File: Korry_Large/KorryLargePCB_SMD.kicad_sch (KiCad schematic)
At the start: 9 parts, among them J1 BTN+LED, J2 BK_LED

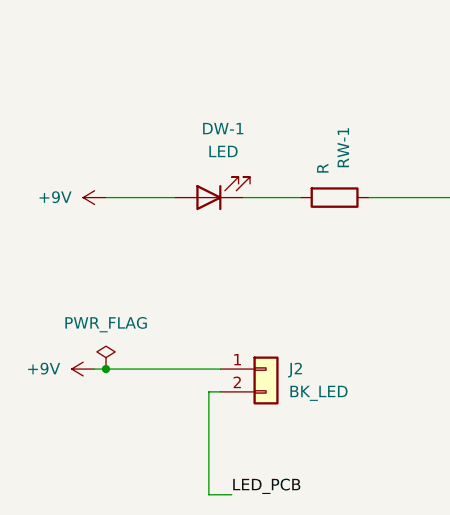
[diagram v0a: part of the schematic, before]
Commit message: Fix the swapped EFIS filenames and rename the backlight nets to +5V
Two naming defects, no electrical change on any board.

EFIS sheets
-----------
The root sheet pointed EFIS_LEFT at efis_right.kicad_sch and EFIS_RIGHT at
efis_left.kicad_sch. The schematic was correct, since the file behind the
LEFT sheet did hold the L_* signals, but the filenames said the opposite and
anyone reading the files from outside KiCad would have been misled.

The two files are swapped and every reference follows: the sheet properties
in the root schematic and the 49 sheetfile entries the footprints carry on
the board. Each file now matches the sheet that loads it.

  netlist   198 nets, 135 components, not one node moved
  ERC       0 violations
  DRC       6 violations, all cosmetic, 0 unconnected, 0 parity issues

Backlight nets
--------------
Every net in the backlighting chain was called +9V while carrying 5 V, on
all four boards. The white LEDs sit behind 91 Ω: at 5 V that is 21 mA, right
at the rating for a 1206 white LED, while 9 V would put them at 65 mA. The
name was a leftover from an earlier design and was the kind of label that
eventually makes someone connect the wrong supply.

Renamed across Korry_Large, Korry_Small, Backlighting_Dimmer and
Backlighting_LEDModule, in both the schematics and the boards: the power
symbol, its value, which is what actually names the net, and the net entries
on the copper. 88 occurrences. None of those boards had a +5V net already,
so nothing was merged.

Verified against the state committed a moment ago: ERC and DRC counts are
identical on all four boards, before and after, and no board gained or lost
a connection.

The Readme drops these two entries and gains the defects that surfaced while
checking: the Backlighting_Dimmer footprints carry their reference in the
value field instead of the schematic value, so a BOM read from that board is
wrong; its terminal block footprint no longer exists in the KiCad library;
four texts on the Korry_Large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
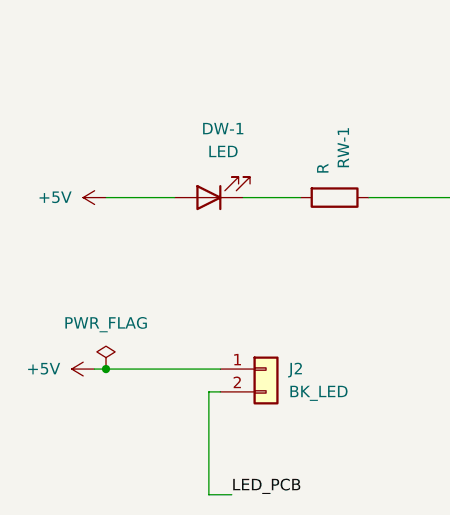
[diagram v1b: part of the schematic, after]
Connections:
- net +9V renamed +5V
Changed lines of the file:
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@@
 	)
 	(symbol
-		(lib_id "power:+9V")
+		(lib_id "power:+5V")
 		(at 72.39 99.06 90)
 		(unit 1)
@@
 			)
 		)
-		(property "Value" "+9V"
+		(property "Value" "+5V"
 			(at 68.58 99.06 90)
 			(effects
@@
 	)
 	(symbol
-		(lib_id "power:+9V")
+		(lib_id "power:+5V")
 		(at 71.12 118.11 90)
 		(unit 1)
@@
 			)
 		)
-		(property "Value" "+9V"
+		(property "Value" "+5V"
 			(at 67.31 118.11 90)
 			(effects

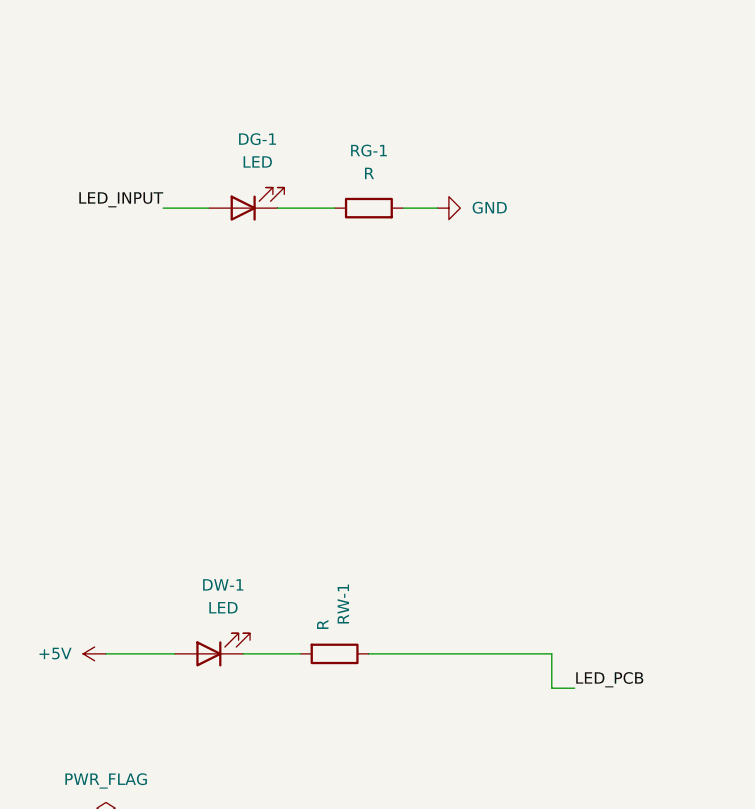
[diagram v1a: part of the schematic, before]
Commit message: Re-annotate the dimmer against its board, set the Korry resistor values
Tidying only. No board changed, no connection moved: all six projects still
report 0 unconnected items and 0 schematic parity issues.

Backlighting_Dimmer was worse than the value mismatch the Readme recorded.
Its schematic and its board disagreed on six reference designators, and
three separate connectors in the schematic all carried J73:

  J73 -> J12, J13, J14     three connectors sharing one reference
  J12 -> J31               J12 was the potentiometer in the schematic and a
                           terminal block on the board
  J93 -> J32
  U2  -> U1

Running Update PCB from Schematic on that board would have pushed those
references onto the copper and left three footprints called J73, against a
silkscreen that is already manufactured. The board is physical reality, so
the schematic was back-annotated from it, values included: R 5K became 5K,
C 470nF became 470nF and so on, which is also the better BOM text.
Schematic parity on that board goes from 6 to 0.

Backlighting_LEDModule had the same problem on one symbol, J73 -> J11.

The Korry resistors had no value in either schematic. Set to the fitted
parts, in the schematics and on the boards: RG 220 ohm for the green
annunciator, RW 91 ohm for the white backlight LED. At 5 V that is about
11 mA and 21 mA.

Three findings are deliberately left as they are, and the Readme now says
why rather than listing them as things to do:

- the dangling terminal block footprint has no replacement in KiCad 10,
  which ships no 2-pin 5.08 mm terminal block. Retargeting it would change
  the pads of a board already made
- the unmirrored + and - markers on the Korry_Large back silkscreen are
  symmetric glyphs, so nothing reads wrong, and mirroring them would move
  them sideways
- the PWR_FLAG the LEDModule wants is a two-click job in Eeschema. That
  file is KiCad 8 and the symbol definition would have to come from a
  KiCad 10 library carrying five toke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
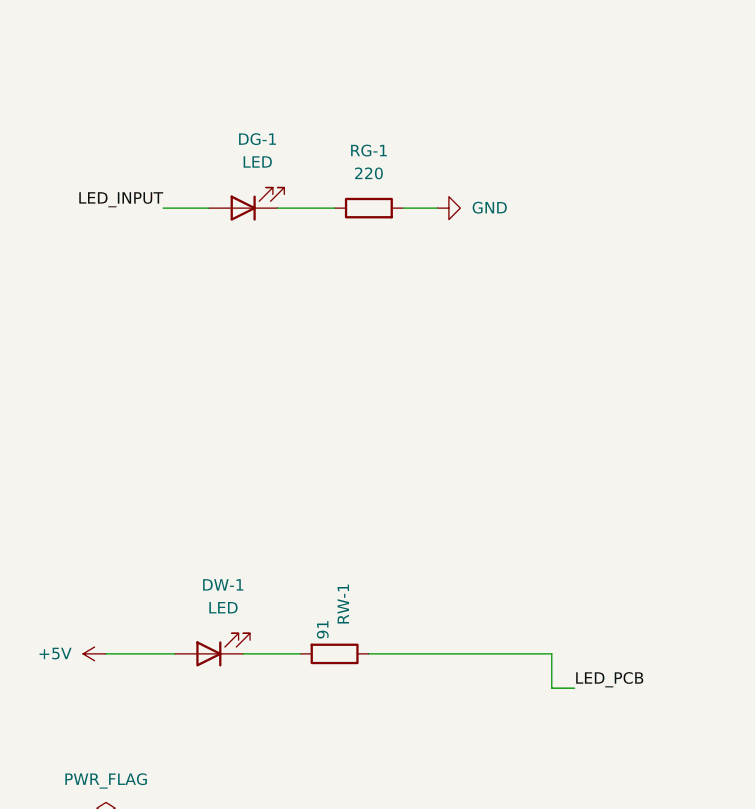
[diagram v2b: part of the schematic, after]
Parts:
- RG-1: value R -> 220
- RW-1: value R -> 91
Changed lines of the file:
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@@
 			)
 		)
-		(property "Value" "R"
+		(property "Value" "91"
 			(at 96.52 95.25 0)
 			(effects
@@
 			)
 		)
-		(property "Value" "R"
+		(property "Value" "220"
 			(at 101.6 45.72 90)
 			(effects

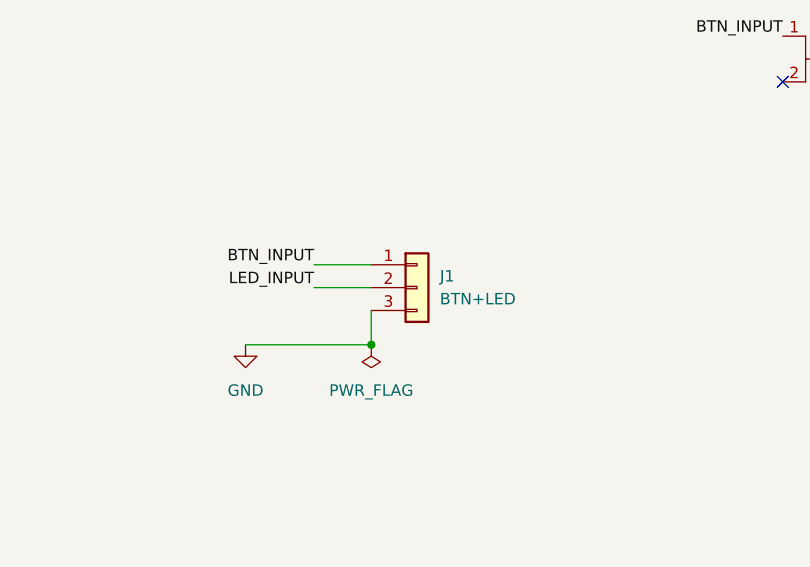
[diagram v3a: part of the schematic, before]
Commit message: Align the Korry connector with the mainboard
La mainboard mette GND sul pin 1 di tutti e 34 i suoi connettori a 3 pin. I
Korry avevano pin 1 = pulsante e pin 3 = GND, quindi con un cavetto dritto
la massa finiva sull'ingresso del pulsante e l'ingresso del multiplexer
sulla massa del Korry. Funzionava solo infilando il connettore al
contrario.

Scambiati i pin 1 e 3 sul Korry, che ha un connettore per scheda, e non
sulla mainboard, che ne ha venti e che con GND sul pin 1 e' coerente con se
stessa.

Sullo schema il simbolo di J1 e' specchiato sull'asse X: i pin 1 e 3 si
scambiano di posto e i fili che c'erano finiscono da soli su quello giusto.
Sul rame si sono scambiate le reti dei due pad e si e' rifatta la pista del
pulsante, che ora esce dall'altro capo del connettore; la massa la prende il
piano come prima. Sul Korry grande la pista scansa il pad 3 dello switch,
che e' massa e sta in mezzo.

Scambiate anche le lettere 'G' e 'B' sul serigrafico, che indicano i pin e
sarebbero diventate bugiarde.

Netlist verificata: J1 ora e' 1=GND, 2=LED_INPUT, 3=BTN_INPUT su entrambe.
Le zone sono da riempire.

Co-Authored-By: Claude Opus 5 <noreply@anthropic.com>
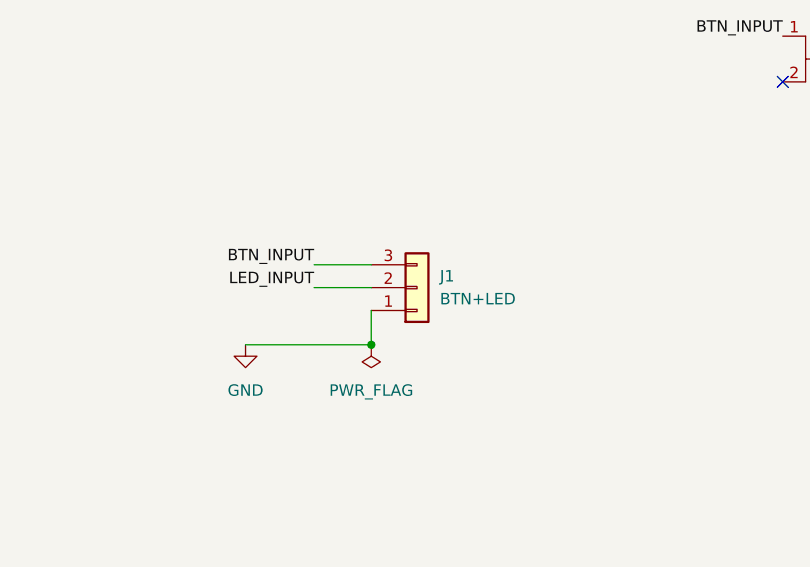
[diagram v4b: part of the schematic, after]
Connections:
- net BTN_INPUT: now also J1.3 (Pin_3); no longer J1.1 (Pin_1)
- net GND: now also J1.1 (Pin_1); no longer J1.3 (Pin_3)
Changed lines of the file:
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@@
 		(lib_id "Connector_Generic:Conn_01x03")
 		(at 190.5 78.74 0)
+		(mirror x)
 		(unit 1)
 		(body_style 1)

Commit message: Keep the last two Digi-Key symbols in the repository
L'ERC segnalava due simboli presi dalla libreria Digi-Key, che non sta nel
Plugin and Content Manager e si scarica a mano da GitHub, per giunta ancora
nel formato .lib di KiCad 5. Per due simboli non vale la pena.

Erano gia' incorporati negli schemi e corretti: mancava solo una libreria a
cui attribuirli. Estratti in due file accanto ai rispettivi progetti, con la
loro sym-lib-table, come si era gia' fatto per il TPS2115A sulla mainboard:

  Backlighting_Dimmer/NE555P.kicad_sym
  Korry_Large/1825910-6.kicad_sym

Sono i simboli con cui le schede sono state disegnate, non equivalenti di
libreria, il che conta soprattutto per il pulsante: Switch:SW_Push_Dual mette
i pin nelle stesse identiche posizioni ma li numera 1-3 e 2-4 dove questo li
numera 1-2 e 3-4, quindi sostituirlo cambierebbe quali pioli sono in corto
dentro al pulsante.

Verificato che i due file sono leggibili da KiCad e che le netlist non si
muovono: NE555 con gli otto pin sulle stesse reti, e sul pulsante pin 1 su
BTN_INPUT, pin 3 su massa, 2 e 4 scollegati come prima.

Sei schede, ERC pulito su tutte. DRC pulito su cinque, piu' l'avviso
serigrafico di J32 sul dimmer. 0 scollegamenti e 0 parita' ovunque.
Delle librerie da installare ne resta una sola, la Alternate KiCad, e serve
per i footprint dei LED e degli Schottky.

Co-Authored-By: Claude Opus 5 <noreply@anthropic.com>
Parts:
- S1: symbol dk_Tactile-Switches:1825910-6 -> 1825910-6:1825910-6
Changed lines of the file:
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@@
 	)
 	(symbol
-		(lib_id "dk_Tactile-Switches:1825910-6")
+		(lib_id "1825910-6:1825910-6")
 		(at 236.22 53.34 0)
 		(unit 1)
